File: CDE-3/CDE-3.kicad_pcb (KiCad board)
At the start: 2 copper layers, 43 parts

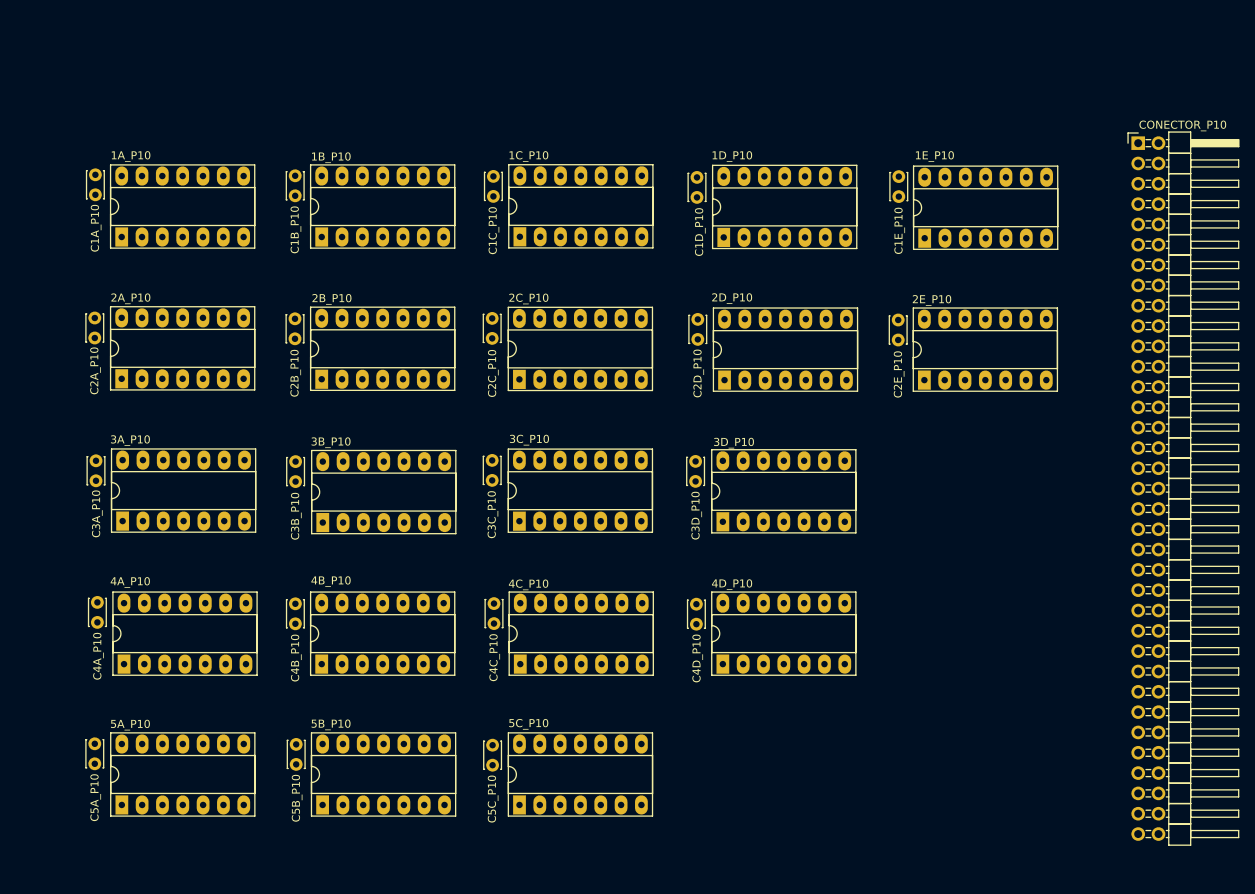
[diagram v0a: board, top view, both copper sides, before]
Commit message: auto-roteamento da placa CDE-3
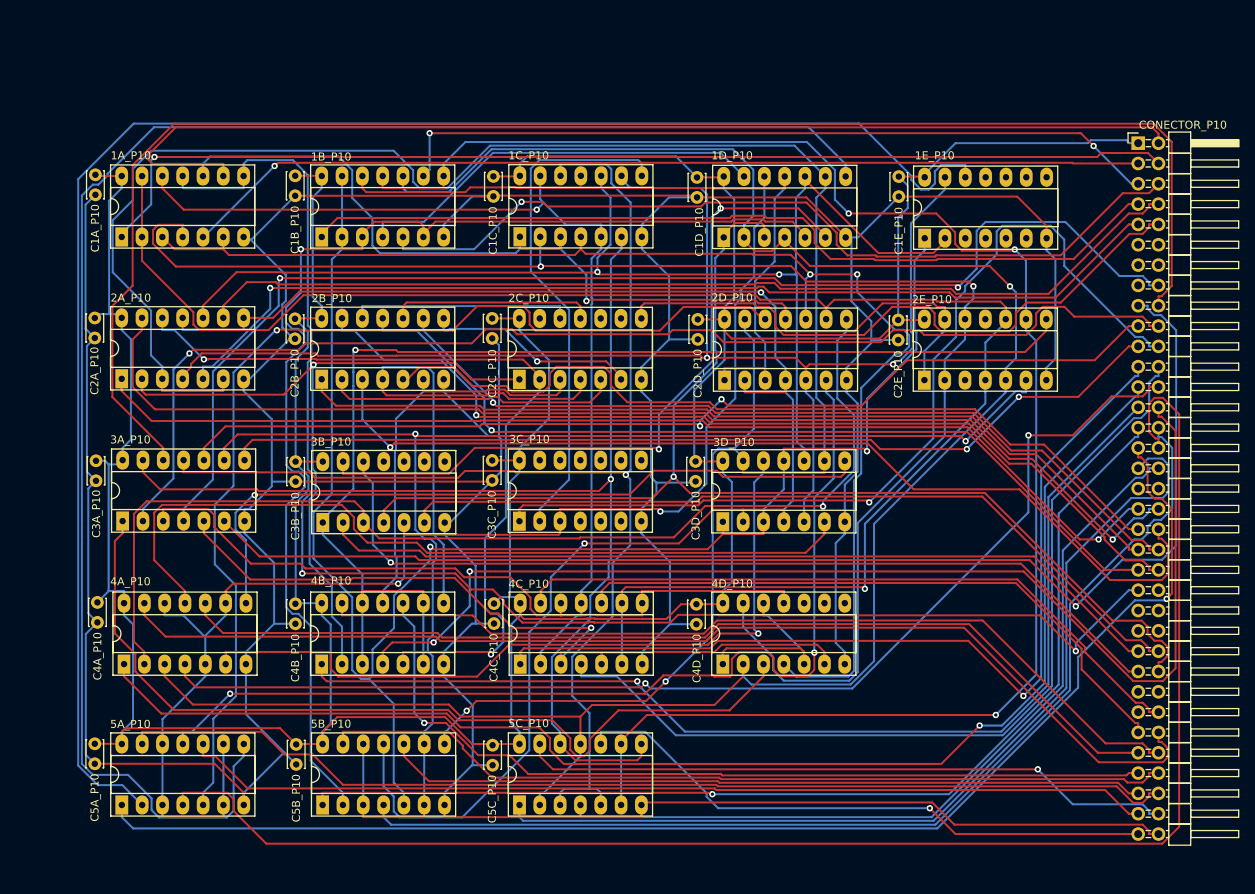
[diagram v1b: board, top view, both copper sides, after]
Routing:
- net GND: track 0.00 -> 676.3 mm
- net VCC: track 0.00 -> 508.0 mm
- net -RI_7: track 0.00 -> 269.5 mm, vias 0 -> 2
- net (+)RI_3: track 0.00 -> 263.3 mm, vias 0 -> 1
- net -RI_3: track 0.00 -> 211.0 mm, vias 0 -> 3
- net -RI_0: track 0.00 -> 210.5 mm, vias 0 -> 2
- net -RI_2: track 0.00 -> 210.0 mm, vias 0 -> 1
- net Net-(1D_P10-Pad8): track 0.00 -> 205.4 mm
- net Net-(1E_P10-Pad12): track 0.00 -> 204.5 mm
- net -RI_6: track 0.00 -> 203.8 mm, vias 0 -> 2
- net -RI_5: track 0.00 -> 201.2 mm, vias 0 -> 2
- net +(SUS+PUG): track 0.00 -> 194.9 mm
- net +ESP-D: track 0.00 -> 193.2 mm
- net (+)RI_1: track 0.00 -> 191.5 mm, vias 0 -> 2
- net Net-(2E_P10-Pad6): track 0.00 -> 174.4 mm, vias 0 -> 2
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
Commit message: limpando a PCB e preparando os planos de terra e as linhas de corte da borda para re-executar o auto-router. Validei também os critérios de largura e espaçamento de trilhas e diametro de vias para estarem de acordo com o que o fornecedor é capaz de produzir.
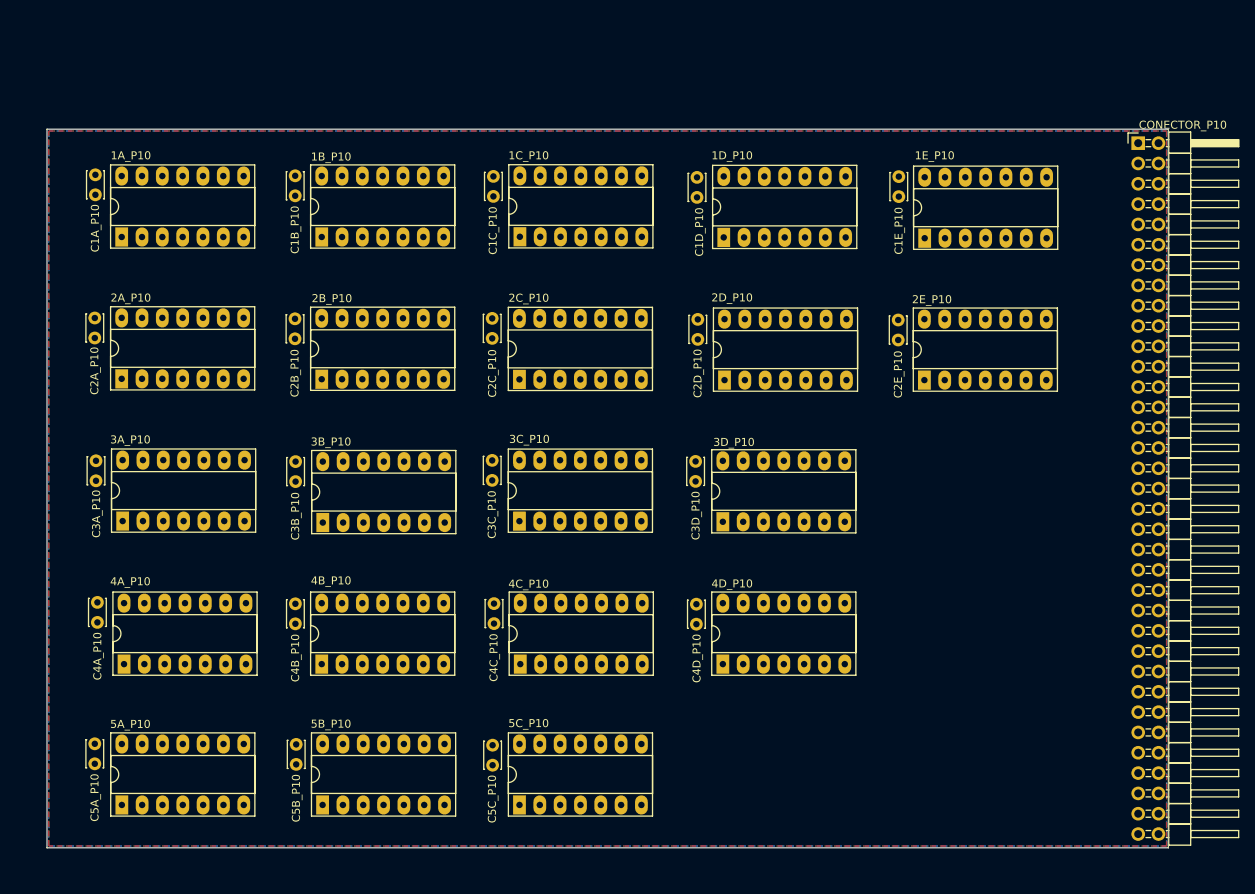
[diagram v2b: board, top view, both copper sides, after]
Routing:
- net GND: track 676.3 -> 0.00 mm
- net VCC: track 508.0 -> 0.00 mm
- net -RI_7: track 269.5 -> 0.00 mm, vias 2 -> 0
- net (+)RI_3: track 263.3 -> 0.00 mm, vias 1 -> 0
- net -RI_3: track 211.0 -> 0.00 mm, vias 3 -> 0
- net -RI_0: track 210.5 -> 0.00 mm, vias 2 -> 0
- net -RI_2: track 210.0 -> 0.00 mm, vias 1 -> 0
- net Net-(1D_P10-Pad8): track 205.4 -> 0.00 mm
- net Net-(1E_P10-Pad12): track 204.5 -> 0.00 mm
- net -RI_6: track 203.8 -> 0.00 mm, vias 2 -> 0
- net -RI_5: track 201.2 -> 0.00 mm, vias 2 -> 0
- net +(SUS+PUG): track 194.9 -> 0.00 mm
- net +ESP-D: track 193.2 -> 0.00 mm
- net (+)RI_1: track 191.5 -> 0.00 mm, vias 2 -> 0
- net Net-(2E_P10-Pad6): track 174.4 -> 0.00 mm, vias 2 -> 0
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- added copper zone on B.Cu, net GND
- added copper zone on F.Cu, net GND
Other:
- board outline added: 140.2 x 89.8 mm

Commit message: tentando novamente com uma área d epcb um pouco maior...
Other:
- board size 140.2 x 89.8 mm -> 145.4 x 96.6 mm
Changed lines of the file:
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@@
   (general
     (links 266)
-    (no_connects 266)
+    (no_connects 225)
     (area 44.6575 23.0425 191.075001 115.9925)
     (thickness 1.6)
@@
     )
   )
-  (gr_line (start 41.75 24.525) (end 41.75 114.35) (layer Edge.Cuts) (width 0.1))
-  (gr_line (start 181.925 24.525) (end 41.75 24.525) (layer Edge.Cuts) (width 0.1))
-  (gr_line (start 181.925 114.35) (end 41.75 114.35) (layer Edge.Cuts) (width 0.1))
-  (gr_line (start 181.925 24.525) (end 181.925 114.35) (layer Edge.Cuts) (width 0.1))
+  (gr_line (start 183.35 118.075) (end 183.35 21.45) (layer Edge.Cuts) (width 0.1))
+  (gr_line (start 37.925 118.075) (end 183.35 118.075) (layer Edge.Cuts) (width 0.1))
+  (gr_line (start 37.925 21.45) (end 37.925 118.075) (layer Edge.Cuts) (width 0.1))
+  (gr_line (start 183.375 21.45) (end 37.925 21.45) (layer Edge.Cuts) (width 0.1))
   (zone (net 10) (net_name GND) (layer B.Cu) (hatch edge 0.508)
     (connect_pads (clearance 0.508))
@@
     (polygon
       (pts
-        (xy 41.975 24.75) (xy 41.975 114.125) (xy 181.7 114.125) (xy 181.7 24.75)
+        (xy 38.275 21.825) (xy 38.275 117.625) (xy 183.025 117.7) (xy 183.075 21.7)
       )
     )
@@
     (polygon
       (pts
-        (xy 181.7 24.75) (xy 181.7 114.125) (xy 41.975 114.125) (xy 41.975 24.75)
+        (xy 183.075 21.7) (xy 183.025 117.7) (xy 38.4 117.6) (xy 38.275 21.825)
       )
     )

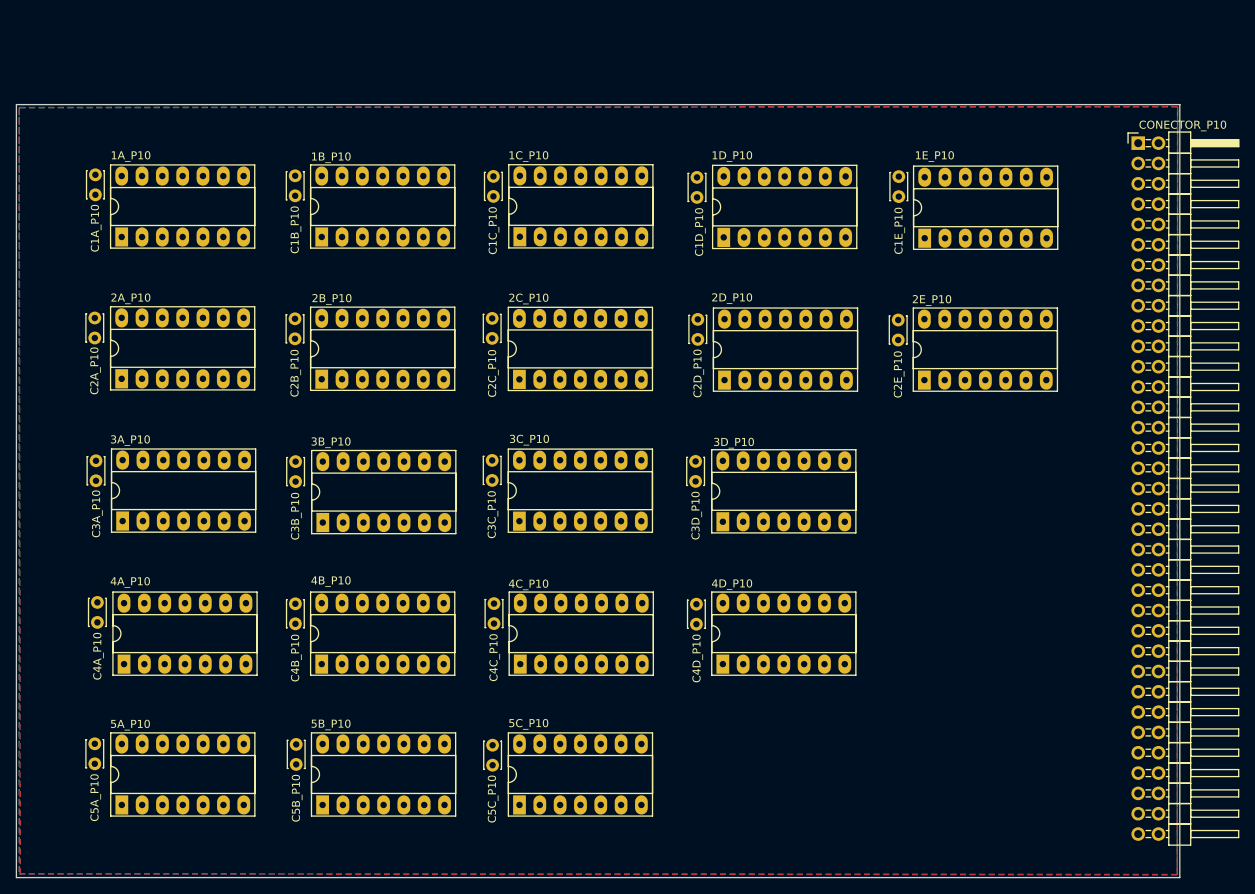
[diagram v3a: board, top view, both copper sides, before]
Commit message: Roteamento automatico com sucesso, placa CDE-3
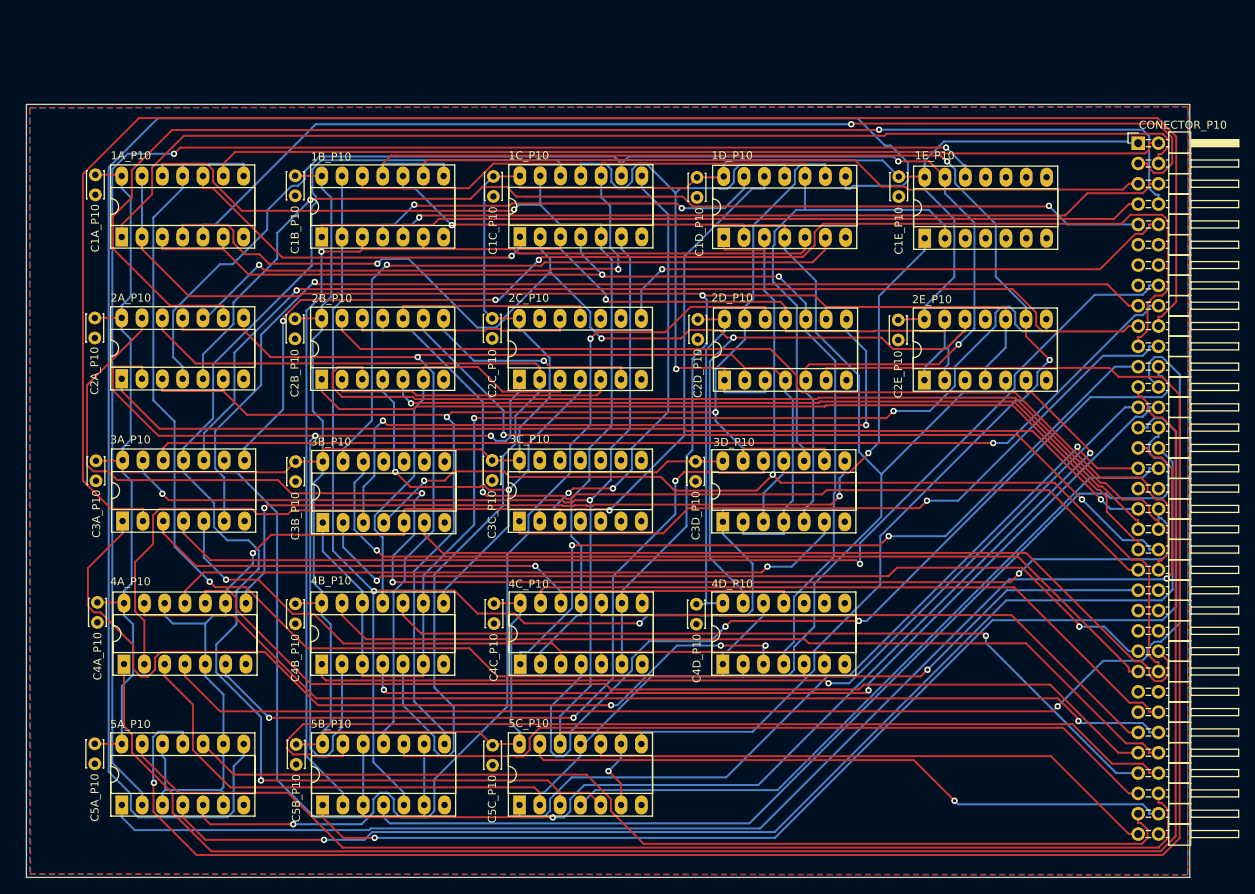
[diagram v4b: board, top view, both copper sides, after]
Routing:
- net VCC: track 0.00 -> 509.9 mm
- net Net-(2D_P10-Pad6): track 0.00 -> 248.8 mm, vias 0 -> 1
- net (+)RI_3: track 0.00 -> 240.7 mm, vias 0 -> 1
- net Net-(1D_P10-Pad8): track 0.00 -> 220.7 mm
- net +INDICE: track 0.00 -> 214.1 mm
- net +MICG1: track 0.00 -> 208.1 mm
- net -RI_0: track 0.00 -> 204.3 mm, vias 0 -> 2
- net -RI_5: track 0.00 -> 203.4 mm, vias 0 -> 3
- net -RI_3: track 0.00 -> 202.8 mm, vias 0 -> 3
- net Net-(2E_P10-Pad6): track 0.00 -> 199.6 mm, vias 0 -> 2
- net Net-(1E_P10-Pad12): track 0.00 -> 191.2 mm, vias 0 -> 2
- net -RI_2: track 0.00 -> 182.8 mm, vias 0 -> 1
- net (+)RI_7: track 0.00 -> 182.4 mm, vias 0 -> 2
- net +RD_1: track 0.00 -> 181.9 mm, vias 0 -> 3
- net -RI_7: track 0.00 -> 179.4 mm, vias 0 -> 2
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
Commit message: CDE-3: adicinando texto descritico à camada de silk superior
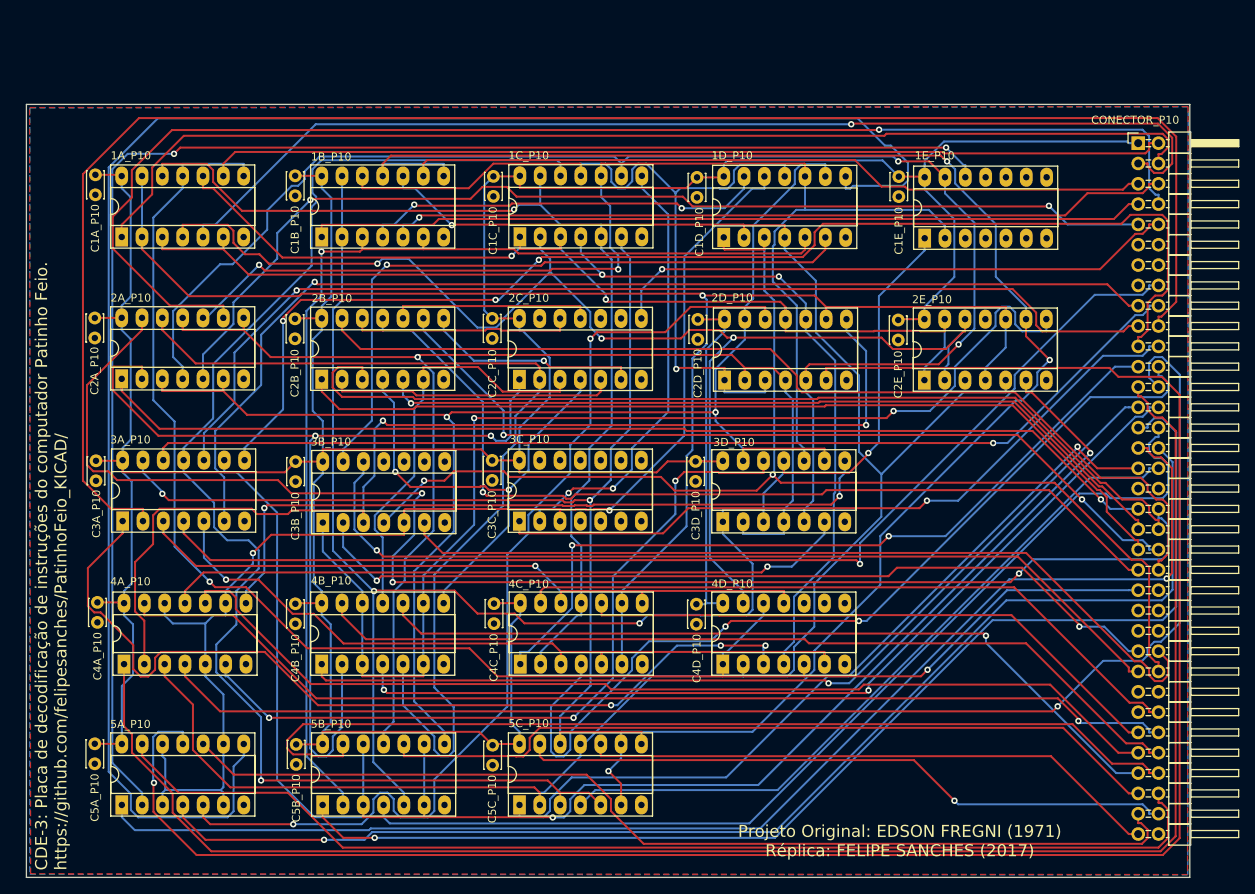
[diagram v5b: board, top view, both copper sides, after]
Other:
- board text added: "CDE-3: Placa de decodificação de instruções do computador Patinho Feio. https://github.com/felipesanches/PatinhoFeio_KICAD/"
- board text added: "Projeto Original: EDSON FREGNI (1971) Réplica: FELIPE SANCHES (2017)"
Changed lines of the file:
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@@
     (area 39.124999 21.374999 184.650001 118.100001)
     (thickness 1.6)
-    (drawings 4)
+    (drawings 6)
     (tracks 1794)
     (zones 0)
@@
     (descr "Through hole angled pin header, 2x35, 2.54mm pitch, 6mm pin length, double rows")
     (tags "Through hole angled pin header THT 2x35 2.54mm double row")
-    (fp_text reference CONECTOR_P10 (at 5.585 -2.27) (layer F.SilkS)
+    (fp_text reference CONECTOR_P10 (at -0.375 -2.895) (layer F.SilkS)
       (effects (font (size 1 1) (thickness 0.15)))
     )
-    (fp_text value CONN_35X2 (at 5.585 88.63) (layer F.Fab)
+    (fp_text value CONN_35X2 (at 1.125 88.905) (layer F.Fab)
       (effects (font (size 1 1) (thickness 0.15)))
     )
@@
     )
   )
+  (gr_text "Projeto Original: EDSON FREGNI (1971)\nRéplica: FELIPE SANCHES (2017)" (at 148.35 113.5) (layer F.SilkS)
+    (effects (font (size 1.5 1.5) (thickness 0.3)))
+  )
+  (gr_text "CDE-3: Placa de decodificação de instruções do computador Patinho Feio.\nhttps://github.com/felipesanches/PatinhoFeio_KICAD/" (at 42.275 117.175 90) (layer F.SilkS)
+    (effects (font (size 1.5 1.5) (thickness 0.3)) (justify left))
+  )
   (gr_line (start 184.6 21.425) (end 39.175 21.425) (layer Edge.Cuts) (width 0.1))
